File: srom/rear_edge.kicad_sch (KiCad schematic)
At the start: 2 parts, among them SW401 SW_SPST

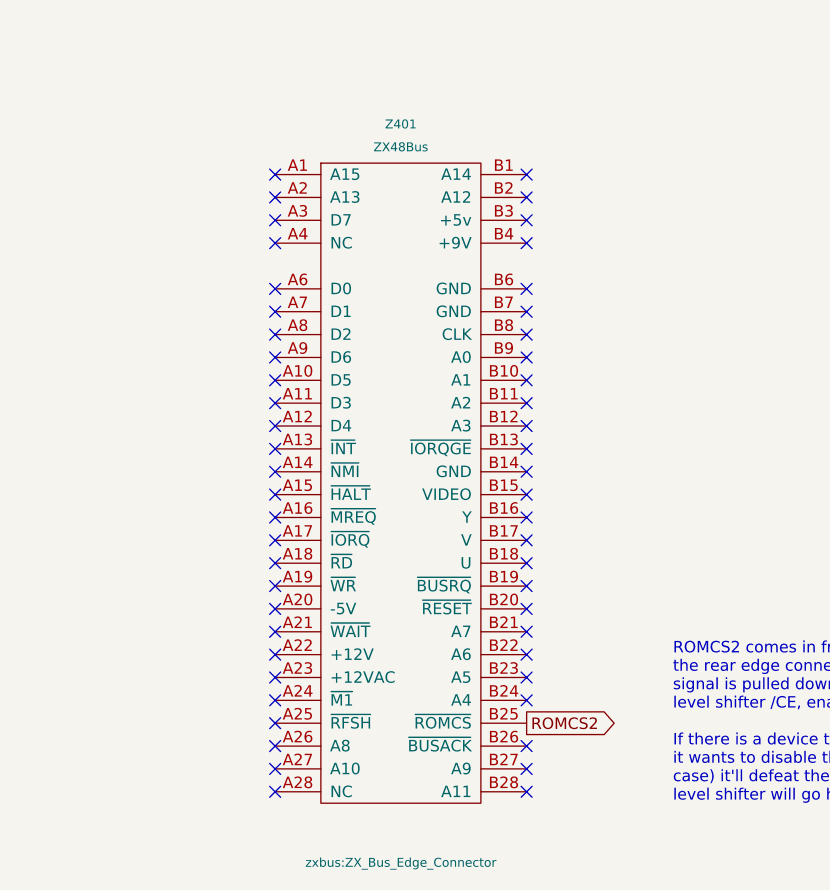
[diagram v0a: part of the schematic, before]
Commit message: board layout work, 4 layers
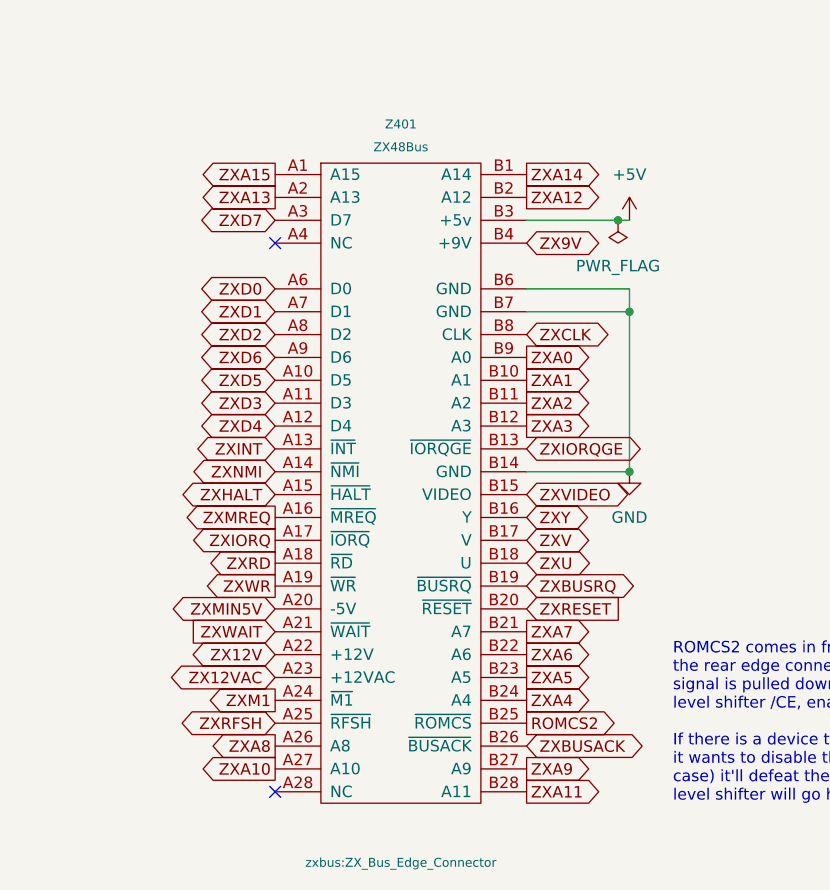
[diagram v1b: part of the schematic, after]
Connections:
- net GND: now also Z401.B14 (GND), Z401.B6 (GND), Z401.B7 (GND)
- net ZXA15: now reaches Z401.A1 (A15)
- net ZXD5: now reaches Z401.A10 (D5)
- net ZXD3: now reaches Z401.A11 (D3)
- net ZXD4: now reaches Z401.A12 (D4)
- net ZXINT: now reaches Z401.A13 (~{INT})
- net ZXNMI: now reaches Z401.A14 (~{NMI})
- net ZXHALT: now reaches Z401.A15 (~{HALT})
- net ZXMREQ: now reaches Z401.A16 (~{MREQ})
- net ZXIORQ: now reaches Z401.A17 (~{IORQ})
- net ZXRD: now reaches Z401.A18 (~{RD})
- net ZXWR: now reaches Z401.A19 (~{WR})
- net ZXA13: now reaches Z401.A2 (A13)
- net ZXMIN5V: now reaches Z401.A20 (-5V)
- net ZXWAIT: now reaches Z401.A21 (~{WAIT})
- net ZX12V: now reaches Z401.A22 (+12V)
- net ZX12VAC: now reaches Z401.A23 (+12VAC)
- net ZXM1: now reaches Z401.A24 (~{M1})
- net ZXRFSH: now reaches Z401.A25 (~{RFSH})
- net ZXA8: now reaches Z401.A26 (A8)
- net ZXA10: now reaches Z401.A27 (A10)
- net ZXD7: now reaches Z401.A3 (D7)
- net ZXD0: now reaches Z401.A6 (D0)
- net ZXD1: now reaches Z401.A7 (D1)
- net ZXD2: now reaches Z401.A8 (D2)
- net ZXD6: now reaches Z401.A9 (D6)
- net ZXA14: now reaches Z401.B1 (A14)
- net ZXA1: now reaches Z401.B10 (A1)
- net ZXA2: now reaches Z401.B11 (A2)
- net ZXA3: now reaches Z401.B12 (A3)
- net ZXIORQGE: now reaches Z401.B13 (~{IORQGE})
- net ZXVIDEO: now reaches Z401.B15 (VIDEO)
- net ZXY: now reaches Z401.B16 (Y)
- net ZXV: now reaches Z401.B17 (V)
- net ZXU: now reaches Z401.B18 (U)
- net ZXBUSRQ: now reaches Z401.B19 (~{BUSRQ})
- net ZXA12: now reaches Z401.B2 (A12)
- net ZXRESET: now reaches Z401.B20 (~{RESET})
- net ZXA7: now reaches Z401.B21 (A7)
- net ZXA6: now reaches Z401.B22 (A6)
- net ZXA5: now reaches Z401.B23 (A5)
- net ZXA4: now reaches Z401.B24 (A4)
- net ZXBUSACK: now reaches Z401.B26 (~{BUSACK})
- net ZXA9: now reaches Z401.B27 (A9)
- net ZXA11: now reaches Z401.B28 (A11)
- net +5V: now reaches Z401.B3 (+5v)
- net ZX9V: now reaches Z401.B4 (+9V)
- net ZXCLK: now reaches Z401.B8 (CLK)
- net ZXA0: now reaches Z401.B9 (A0)
- no-connect marks 53 -> 2
